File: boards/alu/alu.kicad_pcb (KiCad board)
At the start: 2 copper layers, 90 x 100 mm, 81 parts, among them J1 ALU, U1 28C256, U2 74ACT08, U3 28C256, U4 74ACT00, U5 74ACT02

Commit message: PLCC-32 socket footprint
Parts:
- U1, U3: value 28C256 -> AT28C256-PLCC32; footprint Package_LCC:PLCC-28_SMD-Socket -> missing:PLCC-32_SMD_Socket
- moved U3 2.00 mm to (150.0, 91.0)
- moved U1 1.50 mm to (127.5, 91.0)
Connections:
- U1 pad 1: /invert -> (no net)
- U1 pad 10: /a0 -> /a1
- U1 pad 11: /r0 -> /a0
- U1 pad 12: /r1 -> (no net)
- U1 pad 13: /r2 -> /r0
- U1 pad 14: GND -> /r1
- U1 pad 15: /r3 -> /r2
- U1 pad 16: /~carry_lo -> GND
- U1 pad 17: /to_hi -> (no net)
- U1 pad 18: Net-(U1-Pad18) -> /r3
- U1 pad 19: Net-(U1-Pad19) -> /~carry_lo
- U1 pad 2: /carry_in -> /invert
- U1 pad 20: GND -> /to_hi
- U1 pad 21: /op2 -> Net-(U1-Pad21)
- U1 pad 22: /~oe -> Net-(U1-Pad22)
- U1 pad 23: /op3 -> GND
- U1 pad 24: /op1 -> /op2
- U1 pad 25: /op0 -> /~oe
- U1 pad 26: /from_hi -> (no net)
- U1 pad 27: VCC -> /op3
- U1 pad 28: VCC -> /op1
- U1 pad 3: /b3 -> /carry_in
- U1 pad 4: /b2 -> /b3
- U1 pad 5: /b1 -> /b2
- U1 pad 6: /b0 -> /b1
- U1 pad 7: /a3 -> /b0
- U1 pad 8: /a2 -> /a3
- U1 pad 9: /a1 -> /a2
- U3 pad 1: /invert -> (no net)
- U3 pad 10: /a4 -> /a5
- U3 pad 11: /r4 -> /a4
- U3 pad 12: /r5 -> (no net)
- U3 pad 13: /r6 -> /r4
- U3 pad 14: GND -> /r5
- U3 pad 15: /flags2 -> /r6
- U3 pad 16: /~carry_hi -> GND
- U3 pad 17: /to_lo -> (no net)
- U3 pad 18: /flags3 -> /flags2
- U3 pad 19: Net-(U3-Pad19) -> /~carry_hi
- U3 pad 2: /carry_in -> /invert
- U3 pad 20: GND -> /to_lo
- U3 pad 21: /op2 -> /flags3
- U3 pad 22: /~oe -> Net-(U3-Pad22)
- U3 pad 23: /op3 -> GND
- U3 pad 24: /op1 -> /op2
- U3 pad 25: /op0 -> /~oe
- U3 pad 26: /from_lo -> (no net)
- U3 pad 27: VCC -> /op3
- U3 pad 28: VCC -> /op1
- U3 pad 3: /b7 -> /carry_in
- U3 pad 4: /b6 -> /b7
- U3 pad 5: /b5 -> /b6
- U3 pad 6: /b4 -> /b5
- U3 pad 7: /a7 -> /b4
- U3 pad 8: /a6 -> /a7
- U3 pad 9: /a5 -> /a6
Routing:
- net /carry_in: track 57.9 -> 93.4 mm, vias 1 -> 2
- net /invert: track 55.3 -> 87.6 mm, vias 1 -> 2
- net VCC: track 264.9 -> 240.4 mm
- net /flags3: track 90.0 -> 103.9 mm, vias 1 -> 4
- net /op3: track 149.8 -> 145.1 mm, vias 8 -> 6
- net /op0: track 100.6 -> 96.2 mm
- net /~carry_lo: track 26.3 -> 21.9 mm
- net /to_hi: track 31.8 -> 27.7 mm
- net /from_lo: track 44.0 -> 41.1 mm
- net /op1: track 106.6 -> 104.1 mm
- net /r0: track 98.6 -> 96.2 mm
- net /flags2: track 142.3 -> 140.0 mm
- net /op2: track 115.6 -> 117.8 mm, vias 4 -> 6
- net /b4: track 102.5 -> 100.4 mm
- net /~carry_hi: track 17.4 -> 19.4 mm
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
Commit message: Part names
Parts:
- D1, D10, D11, D12, D13, D14, D15, D16, D2, D25, D26, D27, D28, D3, D33, D4, D5, D6, D7, D8, D9: value LED -> KP-2012CGCK
- D17, D18, D19, D20, D21, D22, D23, D24, D29, D30, D31, D32: value LED -> KP-2012EC
- R1, R10, R11, R12, R13, R14, R15, R16, R2, R25, R26, R27, R28, R3, R33, R4, R5, R6, R7, R8, R9: value LED 5mA -> 600
- R17, R18, R19, R20, R21, R22, R23, R24, R29, R30, R31, R32: value LED 5mA -> 620
- U2: value 74ACT08 -> SN74ACT08PW
- U4: value 74ACT00 -> 74ACT00MTCX; footprint Package_SO:SOIC-14_3.9x8.7mm_P1.27mm -> Package_SO:TSSOP-14_4.4x5mm_P0.65mm
- moved U4 0.75 mm to (136.5, 106.0)
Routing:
- net /~z: track 13.4 -> 6.88 mm
- net /~op3: track 12.5 -> 16.3 mm
- net GND: track 89.2 -> 86.6 mm, vias 42 -> 43
- net /z47: track 18.8 -> 21.1 mm
- net /flags0: track 98.7 -> 100.7 mm
- net /op3: track 145.1 -> 146.7 mm
- net /z03: track 18.2 -> 19.5 mm
- net /flags1: track 106.2 -> 107.1 mm
- net VCC: track 240.4 -> 239.8 mm
- added copper zone on F.Cu, net VCC

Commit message: Update net lists and PCBs with new part names
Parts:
- J1: value ALU -> 61304021021
- U5: value 74ACT02 -> MC74ACT02DTR2G
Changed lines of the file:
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@@
       (effects (font (size 1 1) (thickness 0.15)) (justify mirror))
     )
-    (fp_text value ALU (at 5.655 -50.53) (layer B.Fab)
+    (fp_text value 61304021021 (at 5.655 -50.53) (layer B.Fab)
       (effects (font (size 1 1) (thickness 0.15)) (justify mirror))
     )
@@
       (effects (font (size 1 1) (thickness 0.15)))
     )
-    (fp_text value 74ACT02 (at 0 3.55) (layer F.Fab)
+    (fp_text value MC74ACT02DTR2G (at 0 3.55) (layer F.Fab)
       (effects (font (size 1 1) (thickness 0.15)))
     )

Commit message: Add license information
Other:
- board text added: "Licensed under the TAPR OHL (www.tapr.org/OHL)"
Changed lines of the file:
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@@
   (general
     (thickness 1.6)
-    (drawings 23)
+    (drawings 24)
     (tracks 976)
     (zones 0)
@@
   )
   (page A4)
+  (title_block
+    (comment 1 "Licensed under the TAPR Open Hardware License (www.tapr.org/OHL)")
+  )
   (layers
     (0 F.Cu signal)
@@
     )
   )
+  (gr_text "Licensed under the TAPR OHL\n(www.tapr.org/OHL)" (at 172.2 81.8) (layer B.SilkS)
+    (effects (font (size 1 1) (thickness 0.15)) (justify mirror))
+  )
   (dimension 11 (width 0.15) (layer Cmts.User)

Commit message: ALU board started
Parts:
- removed D1, D10, D11, D12, D13, D14, D15, D16, D2, D3, D4, D5, D6, D7, D8, D9: KP-2012CGCK, LED_SMD:LED_0805_2012Metric
- removed D17, D18, D19, D20, D21, D22, D23, D24: KP-2012EC, LED_SMD:LED_0805_2012Metric
- removed R1, R10, R11, R12, R13, R14, R15, R16, R2, R3, R4, R5, R6, R7, R8, R9: 600, Resistor_SMD:R_0805_2012Metric
- removed R17, R18, R19, R20, R21, R22, R23, R24: 620, Resistor_SMD:R_0805_2012Metric
- added C10: 0.1u, Capacitor_SMD:C_0805_2012Metric, F.Cu at (216.8, 75.5)
- added C11: 0.1u, Capacitor_SMD:C_0805_2012Metric, F.Cu at (221.2, 75.5)
- added C6: 0.1u, Capacitor_SMD:C_0805_2012Metric, F.Cu at (230.6, 114.0)
- added C7: 0.1u, Capacitor_SMD:C_0805_2012Metric, F.Cu at (250.6, 90.5)
- added C8: 0.1u, Capacitor_SMD:C_0805_2012Metric, F.Cu at (226.2, 113.9)
- added C9: 0.1u, Capacitor_SMD:C_0805_2012Metric, F.Cu at (226.2, 110.9)
- added U10: 74ACT244MTC, Package_SO:TSSOP-20_4.4x6.5mm_P0.65mm, F.Cu at (136.8, 70.2)
- added U11: 74ACT32MTCX, Package_SO:TSSOP-14_4.4x5mm_P0.65mm, F.Cu at (124.9, 55.4)
- added U12: MC74ACT138DTR2G, Package_SO:TSSOP-16_4.4x5mm_P0.65mm, F.Cu at (144.8, 55.4)
- added U13: SN74ACT08PW, Package_SO:TSSOP-14_4.4x5mm_P0.65mm, F.Cu at (167.2, 55.2)
- added U14: MC74ACT02DTR2G, Package_SO:TSSOP-14_4.4x5mm_P0.65mm, F.Cu at (177.4, 55.2)
- added U15: SN74ACT08PW, Package_SO:TSSOP-14_4.4x5mm_P0.65mm, F.Cu at (146.8, 142.0)
- added U16: 74ACT244MTC, Package_SO:TSSOP-20_4.4x6.5mm_P0.65mm, F.Cu at (177.4, 70.2)
- added U17: 74ACT244MTC, Package_SO:TSSOP-20_4.4x6.5mm_P0.65mm, F.Cu at (167.3, 70.2)
- added U18: 74ACT244MTC, Package_SO:TSSOP-20_4.4x6.5mm_P0.65mm, F.Cu at (126.6, 70.2)
- added U19: 74ACT244MTC, Package_SO:TSSOP-20_4.4x6.5mm_P0.65mm, F.Cu at (116.5, 70.2)
- added U20: 74ACT244MTC, Package_SO:TSSOP-20_4.4x6.5mm_P0.65mm, F.Cu at (147.0, 70.2)
- added U21: SN74ACT240PWR, Package_SO:TSSOP-20_4.4x6.5mm_P0.65mm, F.Cu at (157.1, 70.2)
- added U22: MC74ACT86DG, Package_SO:SOIC-14_3.9x8.7mm_P1.27mm, F.Cu at (160.0, 113.8)
- added U23: MC74ACT86DG, Package_SO:SOIC-14_3.9x8.7mm_P1.27mm, F.Cu at (160.0, 104.0)
- added U24: MC74ACT86DG, Package_SO:SOIC-14_3.9x8.7mm_P1.27mm, F.Cu at (160.0, 94.2)
- added U25: MC74ACT86DG, Package_SO:SOIC-14_3.9x8.7mm_P1.27mm, F.Cu at (160.0, 84.4)
- added U26: MC74ACT86DG, Package_SO:SOIC-14_3.9x8.7mm_P1.27mm, F.Cu at (171.4, 113.8)
- added U27: MC74ACT86DG, Package_SO:SOIC-14_3.9x8.7mm_P1.27mm, F.Cu at (171.4, 104.0)
- added U28: MC74ACT86DG, Package_SO:SOIC-14_3.9x8.7mm_P1.27mm, F.Cu at (171.4, 94.2)
- added U29: MC74ACT86DG, Package_SO:SOIC-14_3.9x8.7mm_P1.27mm, F.Cu at (171.4, 84.4)
- added U30: SN74ACT08PW, Package_SO:TSSOP-14_4.4x5mm_P0.65mm, F.Cu at (147.2, 113.1)
- added U31: SN74ACT08PW, Package_SO:TSSOP-14_4.4x5mm_P0.65mm, F.Cu at (147.6, 82.5)
- added U32: SN74ACT08PW, Package_SO:TSSOP-14_4.4x5mm_P0.65mm, F.Cu at (147.2, 120.7)
- added U33: SN74ACT08PW, Package_SO:TSSOP-14_4.4x5mm_P0.65mm, F.Cu at (147.6, 90.1)
- added U34: 74ACT32MTCX, Package_SO:TSSOP-14_4.4x5mm_P0.65mm, F.Cu at (147.6, 105.0)
- added U35: 74ACT32MTCX, Package_SO:TSSOP-14_4.4x5mm_P0.65mm, F.Cu at (147.6, 97.6)
- added U36: MC74ACT86DG, Package_SO:SOIC-14_3.9x8.7mm_P1.27mm, F.Cu at (165.6, 143.0)
- added U37: MC74ACT02DTR2G, Package_SO:TSSOP-14_4.4x5mm_P0.65mm, F.Cu at (157.6, 55.2)
- added U38: SN74ACT08PW, Package_SO:TSSOP-14_4.4x5mm_P0.65mm, F.Cu at (134.6, 55.4)
- added U6: MC74AC157DR2G, Package_SO:SOIC-16_3.9x9.9mm_P1.27mm, F.Cu at (181.0, 118.8)
- added U7: MC74AC157DR2G, Package_SO:SOIC-16_3.9x9.9mm_P1.27mm, F.Cu at (181.0, 132.6)
- added U8: 74ACT32MTCX, Package_SO:TSSOP-14_4.4x5mm_P0.65mm, F.Cu at (132.2, 82.6)
- added U9: 74ACT32MTCX, Package_SO:TSSOP-14_4.4x5mm_P0.65mm, F.Cu at (132.2, 91.4)
- C3: value 0.1u -> 10u x 6.3V; footprint Capacitor_SMD:C_0805_2012Metric -> Capacitor_SMD:CP_Elec_4x4.5
- C5: value 10u x 6.3V -> 0.1u; footprint Capacitor_SMD:CP_Elec_4x4.5 -> Capacitor_SMD:C_0805_2012Metric
- D25, D26, D27, D28: value KP-2012CGCK -> KP-2012EC
- D29, D30, D31, D32: value KP-2012EC -> KP-2012CGCK
- R25, R26, R27, R28: value 600 -> 620
- R29, R30, R31, R32: value 620 -> 600
- U1: value AT28C256-PLCC32 -> SN74ACT08PW; footprint missing:PLCC-32_SMD_Socket -> Package_SO:TSSOP-14_4.4x5mm_P0.65mm
- U3: value AT28C256-PLCC32 -> 74ACT244MTC; footprint missing:PLCC-32_SMD_Socket -> Package_SO:TSSOP-20_4.4x6.5mm_P0.65mm
- U4: value 74ACT00MTCX -> MC74AC157DR2G; footprint Package_SO:TSSOP-14_4.4x5mm_P0.65mm -> Package_SO:SOIC-16_3.9x9.9mm_P1.27mm
- U5: value MC74ACT02DTR2G -> MC74AC157DR2G; footprint Package_SO:TSSOP-14_4.4x5mm_P0.65mm -> Package_SO:SOIC-16_3.9x9.9mm_P1.27mm
- moved C4 82.9 mm to (149.1, 157.7)
- moved C3 68.1 mm to (114.8, 134.0), turned to 90 degrees
- moved D29 63.2 mm to (110.8, 159.1)
- moved D30 63.2 mm to (108.8, 159.1)
- moved D31 63.2 mm to (106.8, 159.1)
- moved D32 63.2 mm to (104.8, 159.1)
- moved R29 63.2 mm to (110.8, 163.1)
- moved R30 63.2 mm to (108.8, 163.1)
- moved R31 63.2 mm to (106.8, 163.1)
- moved R32 63.2 mm to (104.8, 163.1)
- moved D25 59.9 mm to (207.0, 25.0)
- moved D26 59.9 mm to (205.0, 25.0)
- moved D27 59.9 mm to (203.0, 25.0)
- moved D28 59.9 mm to (201.0, 25.0)
- moved R25 59.9 mm to (207.0, 21.0)
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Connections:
- D25 pad 2: /op0 -> /flags0
- D26 pad 2: /op1 -> /flags1
- D27 pad 2: /op2 -> /flags2
- D28 pad 2: /op3 -> /flags3
- D29 pad 1: Net-(D29-Pad1) -> /~oe
- D29 pad 2: /flags0 -> Net-(D29-Pad2)
- D30 pad 2: /flags1 -> /op0
- D31 pad 2: /flags2 -> /op1
- D32 pad 2: /flags3 -> /adder_sub
- D33 pad 1: /~oe -> Net-(D33-Pad1)
- D33 pad 2: Net-(D33-Pad2) -> /op3
- J1 pad 29: /op2 -> /adder_sub
- R29 pad 1: GND -> VCC
- R29 pad 2: Net-(D29-Pad1) -> Net-(D29-Pad2)
- R33 pad 1: VCC -> GND
- R33 pad 2: Net-(D33-Pad2) -> Net-(D33-Pad1)
- U1 pad 1: (no net) -> /sa4
- U1 pad 10: /a1 -> /adder_b6
- U1 pad 11: /a0 -> Net-(U1-Pad11)
- U1 pad 12: (no net) -> /sa7
- U1 pad 13: /r0 -> /adder_b7
- U1 pad 14: /r1 -> VCC
- U1 pad 2: /invert -> /adder_b4
- U1 pad 3: /carry_in -> Net-(U1-Pad3)
- U1 pad 4: /b3 -> /sa5
- U1 pad 5: /b2 -> /adder_b5
- U1 pad 6: /b1 -> Net-(U1-Pad6)
- U1 pad 7: /b0 -> GND
- U1 pad 8: /a3 -> Net-(U1-Pad8)
- U1 pad 9: /a2 -> /sa6
- U2 pad 1: /op3 -> /sa0
- U2 pad 10: /nor23 -> /adder_b2
- U2 pad 11: /z47 -> Net-(U2-Pad11)
- U2 pad 12: /nor45 -> /sa3
- U2 pad 13: /nor67 -> /adder_b3
- U2 pad 2: /to_lo -> /sb0
- U2 pad 3: /from_hi -> Net-(U2-Pad3)
- U2 pad 4: /~op3 -> /sa1
- U2 pad 5: /to_hi -> /adder_b1
- U2 pad 6: /from_lo -> Net-(U2-Pad6)
- U2 pad 8: /z03 -> Net-(U2-Pad8)
- U2 pad 9: /nor01 -> /sa2
- U3 pad 1: (no net) -> /~and_oe
- U3 pad 10: /a5 -> GND
- U3 pad 11: /a4 -> Net-(U2-Pad11)
- U3 pad 12: (no net) -> /flags2
- U3 pad 13: /r4 -> Net-(U2-Pad8)
- U3 pad 14: /r5 -> /r6
- U3 pad 15: /r6 -> Net-(U2-Pad6)
- U3 pad 16: GND -> /r5
- U3 pad 17: (no net) -> Net-(U2-Pad3)
- U3 pad 18: /flags2 -> /r4
- U3 pad 19: /~carry_hi -> /~and_oe
- U3 pad 2: /invert -> Net-(U1-Pad3)
- U3 pad 20: /to_lo -> VCC
- U3 pad 3: /carry_in -> /r0
- U3 pad 4: /b7 -> Net-(U1-Pad6)
- U3 pad 5: /b6 -> /r1
- U3 pad 6: /b5 -> Net-(U1-Pad8)
- U3 pad 7: /b4 -> /r2
- U3 pad 8: /a7 -> Net-(U1-Pad11)
- U3 pad 9: /a6 -> /r3
- U4 pad 1: /op3 -> /swap
- U4 pad 10: /~z -> /b2
- U4 pad 11: /flags1 -> /a2
- U4 pad 12: /~carry_lo -> /sa3
- U4 pad 13: /~carry_hi -> /b3
- U4 pad 14: VCC -> /a3
- U4 pad 2: /op3 -> /a0
- U4 pad 3: /~op3 -> /b0
- U4 pad 4: /z47 -> /sa0
- U4 pad 5: /z03 -> /a1
- U4 pad 6: /~z -> /b1
- U4 pad 7: GND -> /sa1
- U4 pad 8: /flags0 -> GND
- U4 pad 9: /~z -> /sa2
- U5 pad 1: /nor01 -> /swap
- U5 pad 10: /nor45 -> /b6
- U5 pad 11: /r6 -> /a6
- U5 pad 12: /flags2 -> /sa7
- U5 pad 13: /nor67 -> /b7
- U5 pad 14: VCC -> /a7
- U5 pad 2: /r0 -> /a4
- U5 pad 3: /r1 -> /b4
- U5 pad 4: /nor23 -> /sa4
- U5 pad 5: /r2 -> /a5
- U5 pad 6: /r3 -> /b5
- U5 pad 7: GND -> /sa5
- U5 pad 8: /r4 -> GND
- U5 pad 9: /r5 -> /sa6
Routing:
- net /sa3: track 0.00 -> 236.9 mm, vias 0 -> 12
- net /sa1: track 0.00 -> 233.3 mm, vias 0 -> 14
- net /sa7: track 0.00 -> 232.5 mm, vias 0 -> 15
- net /sa2: track 0.00 -> 228.8 mm, vias 0 -> 12
- net /adder_b4: track 0.00 -> 227.1 mm, vias 0 -> 11
- net /adder_b5: track 0.00 -> 223.3 mm, vias 0 -> 10
- net /sb0: track 0.00 -> 217.7 mm, vias 0 -> 10
- net /adder_b7: track 0.00 -> 215.2 mm, vias 0 -> 9
- net /sa4: track 0.00 -> 213.0 mm, vias 0 -> 12
- net /adder_sub: track 0.00 -> 210.5 mm, vias 0 -> 19
- net /sa5: track 0.00 -> 206.5 mm, vias 0 -> 12
- net /sa0: track 0.00 -> 198.0 mm, vias 0 -> 10
- net /sa6: track 0.00 -> 196.1 mm, vias 0 -> 10
- net /~sa_ena: track 0.00 -> 187.8 mm, vias 0 -> 12
- net /adder_b1: track 0.00 -> 179.4 mm, vias 0 -> 10
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
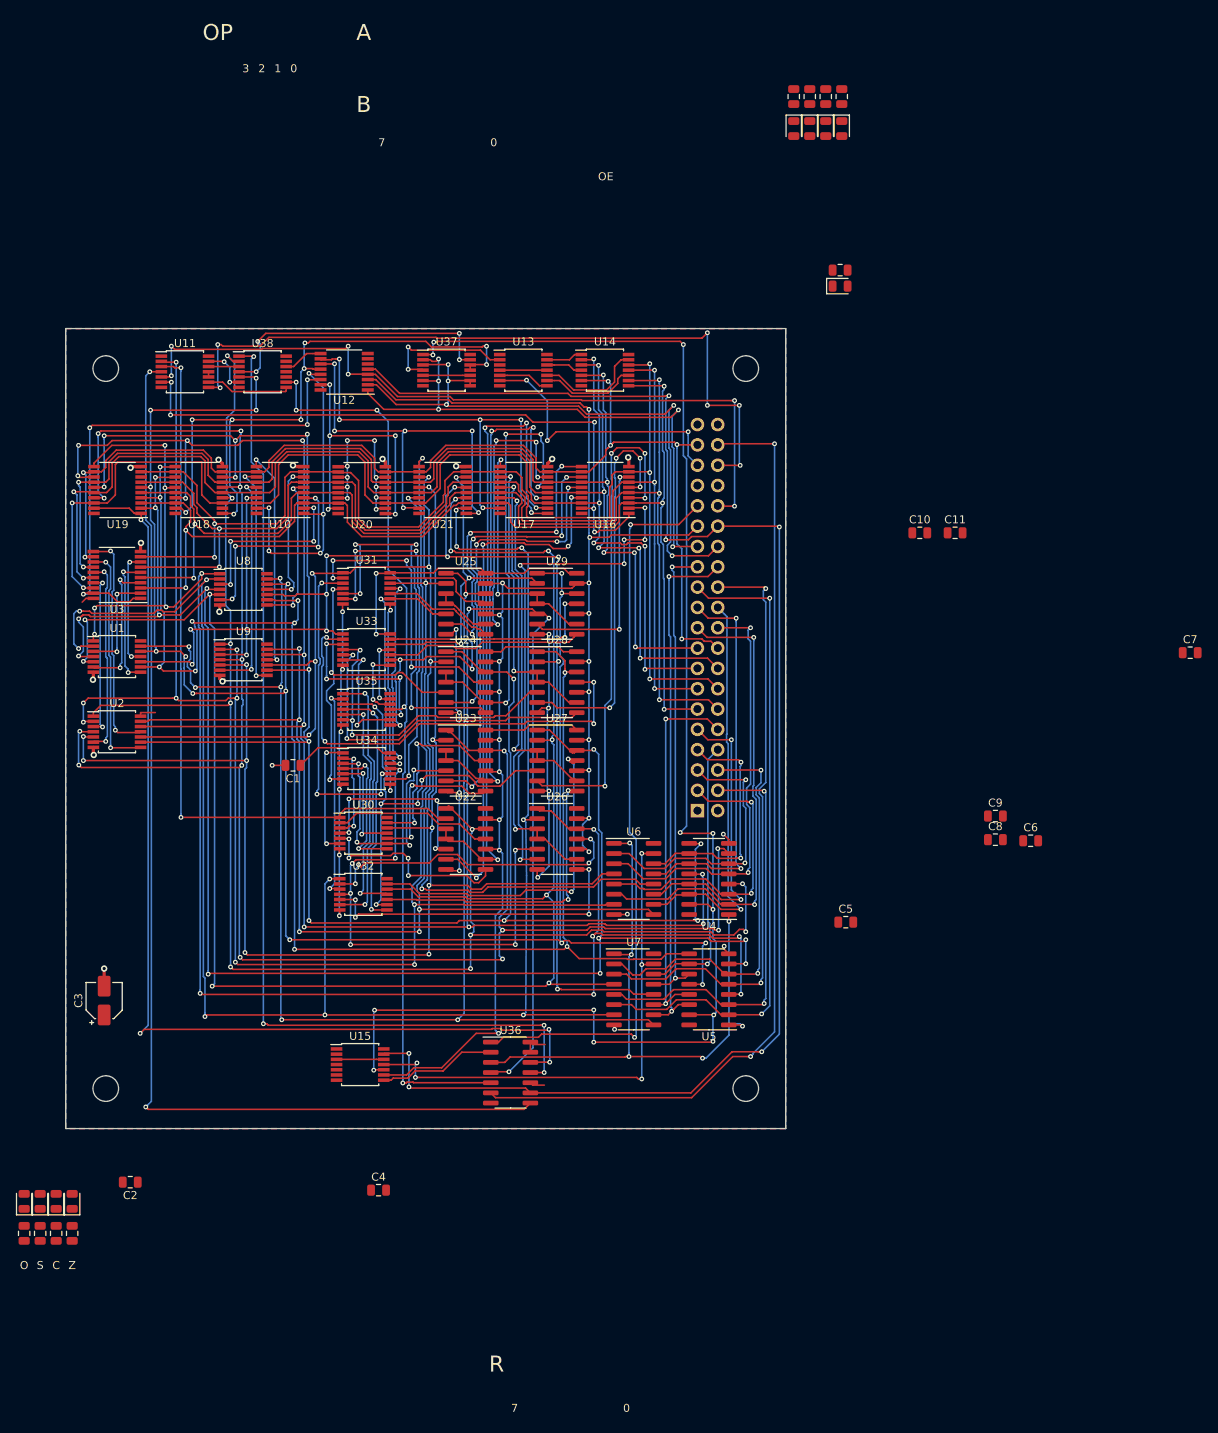
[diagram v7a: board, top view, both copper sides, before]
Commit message: VCC and GND tracks
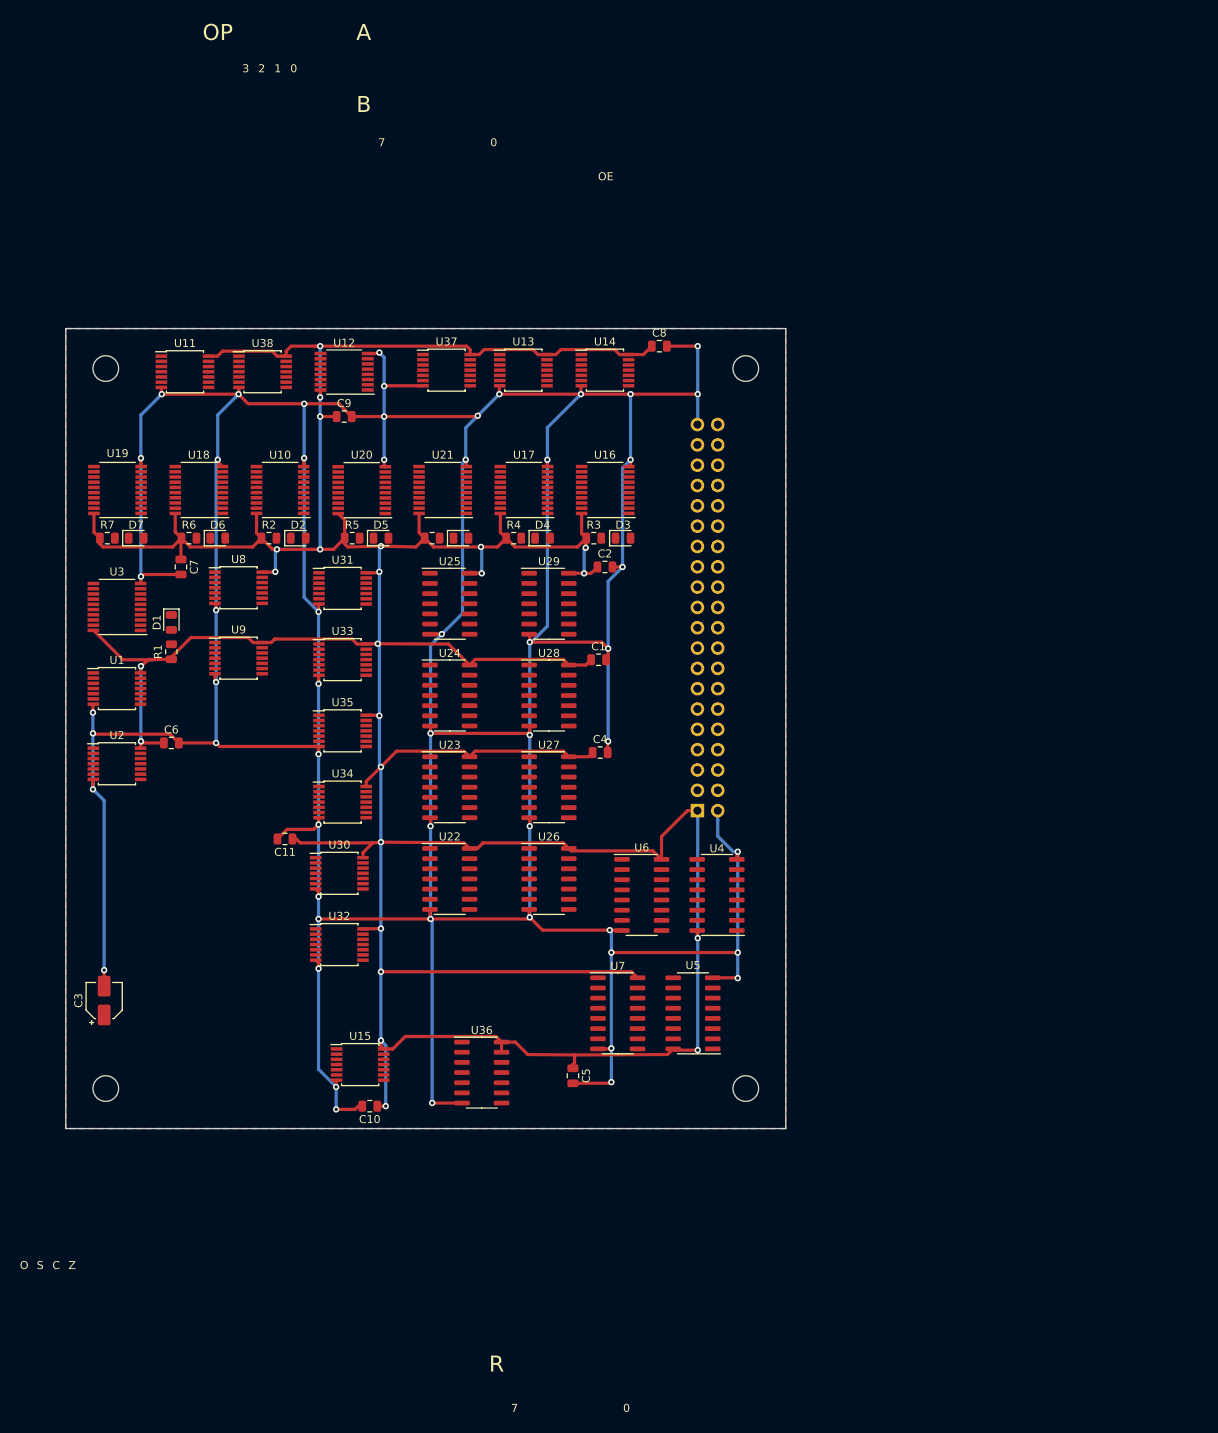
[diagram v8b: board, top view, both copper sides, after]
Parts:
- removed D26, D27, D28: KP-2012EC, LED_SMD:LED_0805_2012Metric
- removed D29, D30, D31, D32, D33: KP-2012CGCK, LED_SMD:LED_0805_2012Metric
- removed R26, R27, R28: 620, Resistor_SMD:R_0805_2012Metric
- removed R29, R30, R31, R32, R33: 600, Resistor_SMD:R_0805_2012Metric
- added D1: KP-2012EC, LED_SMD:LED_0805_2012Metric, F.Cu at (123.2, 86.7)
- added D2: KP-2012EC, LED_SMD:LED_0805_2012Metric, F.Cu at (139.1, 76.2)
- added D3: KP-2012EC, LED_SMD:LED_0805_2012Metric, F.Cu at (179.7, 76.2)
- added D4: KP-2012EC, LED_SMD:LED_0805_2012Metric, F.Cu at (169.6, 76.2)
- added D5: KP-2012EC, LED_SMD:LED_0805_2012Metric, F.Cu at (149.4, 76.2)
- added D6: KP-2012EC, LED_SMD:LED_0805_2012Metric, F.Cu at (129.0, 76.2)
- added D7: KP-2012EC, LED_SMD:LED_0805_2012Metric, F.Cu at (118.8, 76.2)
- added R1: 620, Resistor_SMD:R_0805_2012Metric, F.Cu at (123.2, 90.4)
- added R2: 620, Resistor_SMD:R_0805_2012Metric, F.Cu at (135.4, 76.2)
- added R3: 620, Resistor_SMD:R_0805_2012Metric, F.Cu at (176.0, 76.2)
- added R4: 620, Resistor_SMD:R_0805_2012Metric, F.Cu at (166.0, 76.2)
- added R5: 620, Resistor_SMD:R_0805_2012Metric, F.Cu at (145.8, 76.2)
- added R6: 620, Resistor_SMD:R_0805_2012Metric, F.Cu at (125.4, 76.2)
- added R7: 620, Resistor_SMD:R_0805_2012Metric, F.Cu at (115.2, 76.2)
- moved C7 126.6 mm to (124.4, 79.8), turned to 270 degrees
- moved C6 108.1 mm to (123.2, 101.8)
- moved C10 99.3 mm to (148.0, 147.2), turned to 180 degrees
- moved C2 97.1 mm to (177.4, 79.8), turned to 0 degrees
- moved C9 95.5 mm to (144.8, 61.0)
- moved C11 92.1 mm to (137.4, 113.8), turned to 180 degrees
- moved R8 75.3 mm to (155.8, 76.2), turned to 0 degrees
- moved C8 74.6 mm to (184.2, 52.2)
- moved D8 69.9 mm to (159.4, 76.2), turned to 0 degrees
- moved C4 61.3 mm to (176.8, 103.0)
- moved C1 40.4 mm to (176.6, 91.4), turned to 0 degrees
- moved C5 39.1 mm to (173.4, 143.4), turned to 270 degrees
- moved U32 6.96 mm to (144.2, 127.0)
- moved U30 5.85 mm to (144.2, 118.1)
- moved U22 5.39 mm to (158.0, 118.8)
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- renumbered D25 to D8, R25 to R8
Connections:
- D8 pad 2: /flags0 -> /~not_oe
- R8 pad 1: GND -> VCC
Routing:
- net GND: track 139.1 -> 710.1 mm, vias 32 -> 55
- net VCC: track 80.6 -> 558.9 mm, vias 2 -> 24
- net /sa3: track 236.9 -> 0.00 mm, vias 12 -> 0
- net /sa1: track 233.3 -> 0.00 mm, vias 14 -> 0
- net /sa7: track 232.5 -> 0.00 mm, vias 15 -> 0
- net /sa2: track 228.8 -> 0.00 mm, vias 12 -> 0
- net /adder_b4: track 227.1 -> 0.00 mm, vias 11 -> 0
- net /adder_b5: track 223.3 -> 0.00 mm, vias 10 -> 0
- net /sb0: track 217.7 -> 0.00 mm, vias 10 -> 0
- net /adder_b7: track 215.2 -> 0.00 mm, vias 9 -> 0
- net /sa4: track 213.0 -> 0.00 mm, vias 12 -> 0
- net /adder_sub: track 210.5 -> 0.00 mm, vias 19 -> 0
- net /sa5: track 206.5 -> 0.00 mm, vias 12 -> 0
- net /sa0: track 198.0 -> 0.00 mm, vias 10 -> 0
- net /sa6: track 196.1 -> 0.00 mm, vias 10 -> 0
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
